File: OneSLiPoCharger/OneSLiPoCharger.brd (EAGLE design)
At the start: 101.6 x 52.1 mm, 55 parts, among them IC1 LM358N, Q1 BUZ10

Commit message: Widen isolation. Add ground traces to MCP groups to account for lack of gnd pour. Reduce board width.
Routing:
- net GND: track 0.00 -> 94.4 mm
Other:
- board size 101.6 x 52.1 mm -> 99.1 x 52.1 mm
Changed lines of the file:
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@@
 <grid distance="0.05" unitdist="inch" unit="inch" style="lines" multiple="1" display="no" altdistance="0.025" altunitdist="inch" altunit="inch"/>
 <layers>
-<layer number="1" name="Top" color="4" fill="1" visible="yes" active="yes"/>
-<layer number="16" name="Bottom" color="1" fill="1" visible="yes" active="yes"/>
-<layer number="17" name="Pads" color="2" fill="1" visible="yes" active="yes"/>
-<layer number="18" name="Vias" color="2" fill="1" visible="yes" active="yes"/>
-<layer number="19" name="Unrouted" color="6" fill="1" visible="yes" active="yes"/>
+<layer number="1" name="Top" color="4" fill="1" visible="no" active="yes"/>
+<layer number="16" name="Bottom" color="1" fill="1" visible="no" active="yes"/>
+<layer number="17" name="Pads" color="2" fill="1" visible="no" active="yes"/>
+<layer number="18" name="Vias" color="2" fill="1" visible="no" active="yes"/>
+<layer number="19" name="Unrouted" color="6" fill="1" visible="no" active="yes"/>
 <layer number="20" name="Dimension" color="15" fill="1" visible="yes" active="yes"/>
-<layer number="21" name="tPlace" color="7" fill="1" visible="yes" active="yes"/>
-<layer number="22" name="bPlace" color="7" fill="1" visible="yes" active="yes"/>
-<layer number="23" name="tOrigins" color="15" fill="1" visible="yes" active="yes"/>
-<layer number="24" name="bOrigins" color="15" fill="1" visible="yes" active="yes"/>
+<layer number="21" name="tPlace" color="7" fill="1" visible="no" active="yes"/>
+<layer number="22" name="bPlace" color="7" fill="1" visible="no" active="yes"/>
+<layer number="23" name="tOrigins" color="15" fill="1" visible="no" active="yes"/>
+<layer number="24" name="bOrigins" color="15" fill="1" visible="no" active="yes"/>
 <layer number="25" name="tNames" color="7" fill="1" visible="no" active="yes"/>
 <layer number="26" name="bNames" color="7" fill="1" visible="no" active="yes"/>
@@
 <layer number="43" name="vRestrict" color="2" fill="10" visible="no" active="yes"/>
 <layer number="44" name="Drills" color="7" fill="1" visible="no" active="yes"/>
-<layer number="45" name="Holes" color="7" fill="1" visible="yes" active="yes"/>
+<layer number="45" name="Holes" color="7" fill="1" visible="no" active="yes"/>
 <layer number="46" name="Milling" color="3" fill="1" visible="no" active="yes"/>
 <layer number="47" name="Measures" color="7" fill="1" visible="no" active="yes"/>
@@
 <board>
 <plain>
-<wire x1="101.6" y1="0" x2="101.6" y2="52.07" width="0" layer="20"/>
-<wire x1="101.6" y1="52.07" x2="0" y2="52.07" width="0" layer="20"/>
+<wire x1="99.06" y1="0" x2="99.06" y2="52.07" width="0" layer="20"/>
+<wire x1="99.06" y1="52.07" x2="0" y2="52.07" width="0" layer="20"/>
 <wire x1="0" y1="52.07" x2="0" y2="0" width="0" layer="20"/>
 <text x="53.34" y="29.21" size="1.016" layer="21" rot="R180">BAT1</text>
@@
 <text x="67.31" y="22.86" size="1.016" layer="21">BAT5</text>
 <text x="86.36" y="22.86" size="1.016" layer="21">BAT6</text>
-<text x="97.79" y="22.86" size="1.778" layer="16" rot="MR90">1SLipo v1.0</text>
+<text x="95.25" y="22.86" size="1.778" layer="16" rot="MR90">1SLipo v1.0</text>
 <hole x="2.54" y="2.54" drill="3.2"/>
 <hole x="2.54" y="49.53" drill="3.2"/>
-<hole x="99.06" y="49.53" drill="3.2"/>
-<hole x="99.06" y="2.54" drill="3.2"/>
-<wire x1="101.6" y1="0" x2="0" y2="0" width="0" layer="20"/>
+<hole x="96.52" y="49.53" drill="3.2"/>
+<hole x="96.52" y="2.54" drill="3.2"/>
+<wire x1="99.06" y1="0" x2="0" y2="0" width="0" layer="20"/>
 </plain>
 <attributes>
@@
 <contactref element="U$1" pad="2"/>
 <contactref element="C3" pad="1"/>
-<polygon width="0.6096" layer="16" isolate="0.3048">
+<polygon width="0.6096" layer="16" isolate="0.6096">
 <vertex x="0" y="0"/>
-<vertex x="101.6" y="0"/>
-<vertex x="101.6" y="52.07"/>
+<vertex x="99.06" y="0"/>
+<vertex x="99.06" y="52.07"/>
 <vertex x="0" y="52.07"/>
 </polygon>
@@
 <contactref element="U$13" pad="P$1"/>
 <contactref element="JP1" pad="3"/>
+<wire x1="50.8" y1="41.59" x2="50.48" y2="41.59" width="0.6096" layer="16"/>
+<wire x1="50.48" y1="41.59" x2="46.99" y2="38.1" width="0.6096" layer="16"/>
+<wire x1="46.99" y1="38.1" x2="46.99" y2="37.78" width="0.6096" layer="16"/>
+<wire x1="46.99" y1="37.78" x2="48.58" y2="37.78" width="0.6096" layer="16"/>
+<wire x1="48.58" y1="37.78" x2="49.53" y2="36.83" width="0.6096" layer="16"/>
+<wire x1="49.53" y1="36.83" x2="53.37" y2="36.83" width="0.6096" layer="16"/>
+<wire x1="53.37" y1="36.83" x2="54.61" y2="36.83" width="0.6096" layer="16"/>
+<wire x1="54.61" y1="36.83" x2="55.88" y2="37.78" width="0.6096" layer="16"/>
+<wire x1="64.77" y1="37.78" x2="64.77" y2="38.1" width="0.6096" layer="16"/>
+<wire x1="64.77" y1="38.1" x2="68.26" y2="41.59" width="0.6096" layer="16"/>
+<wire x1="68.26" y1="41.59" x2="68.58" y2="41.59" width="0.6096" layer="16"/>
+<wire x1="71.15" y1="36.83" x2="67.31" y2="36.83" width="0.6096" layer="16"/>
+<wire x1="67.31" y1="36.83" x2="66.36" y2="37.78" width="0.6096" layer="16"/>
+<wire x1="66.36" y1="37.78" x2="64.77" y2="37.78" width="0.6096" layer="16"/>
+<wire x1="71.15" y1="36.83" x2="72.39" y2="36.83" width="0.6096" layer="16"/>
+<wire x1="72.39" y1="36.83" x2="73.66" y2="37.78" width="0.6096" layer="16"/>
+<wire x1="83.82" y1="37.78" x2="83.82" y2="38.1" width="0.6096" layer="16"/>
+<wire x1="83.82" y1="38.1" x2="87.31" y2="41.59" width="0.6096" layer="16"/>
+<wire x1="87.31" y1="41.59" x2="87.63" y2="41.59" width="0.6096" layer="16"/>
+<wire x1="90.2" y1="36.83" x2="86.36" y2="36.83" width="0.6096" layer="16"/>
+<wire x1="86.36" y1="36.83" x2="85.41" y2="37.78" width="0.6096" layer="16"/>
+<wire x1="85.41" y1="37.78" x2="83.82" y2="37.78" width="0.6096" layer="16"/>
+<wire x1="90.2" y1="36.83" x2="91.44" y2="36.83" width="0.6096" layer="16"/>
+<wire x1="91.44" y1="36.83" x2="92.71" y2="37.78" width="0.6096" layer="16"/>
+<wire x1="93.98" y1="14.29" x2="93.98" y2="13.97" width="0.6096" layer="16"/>
+<wire x1="90.17" y1="10.16" x2="90.17" y2="10.48" width="0.6096" layer="16"/>
+<wire x1="87.6" y1="15.24" x2="86.36" y2="15.24" width="0.6096" layer="16"/>
+<wire x1="86.36" y1="15.24" x2="85.41" y2="14.29" width="0.6096" layer="16"/>
+<wire x1="85.41" y1="14.29" x2="85.09" y2="14.29" width="0.6096" layer="16"/>
+<wire x1="68.55" y1="15.24" x2="67.31" y2="15.24" width="0.6096" layer="16"/>
+<wire x1="67.31" y1="15.24" x2="66.36" y2="14.29" width="0.6096" layer="16"/>
+<wire x1="66.36" y1="14.29" x2="66.04" y2="14.29" width="0.6096" layer="16"/>
+<wire x1="68.55" y1="15.24" x2="72.39" y2="15.24" width="0.6096" layer="16"/>
+<wire x1="72.39" y1="15.24" x2="73.34" y2="14.29" width="0.6096" layer="16"/>
+<wire x1="73.34" y1="14.29" x2="74.93" y2="14.29" width="0.6096" layer="16"/>
+<wire x1="74.93" y1="14.29" x2="74.93" y2="12.7" width="0.6096" layer="16"/>
+<wire x1="74.93" y1="12.7" x2="72.71" y2="10.48" width="0.6096" layer="16"/>
+<wire x1="72.71" y1="10.48" x2="71.12" y2="10.48" width="0.6096" layer="16"/>
+<wire x1="87.6" y1="15.24" x2="91.44" y2="15.24" width="0.6096" layer="16"/>
+<wire x1="91.44" y1="15.24" x2="92.39" y2="14.29" width="0.6096" layer="16"/>
+<wire x1="92.39" y1="14.29" x2="93.98" y2="14.29" width="0.6096" layer="16"/>
+<wire x1="90.17" y1="10.48" x2="90.49" y2="10.16" width="0.6096" layer="16"/>
+<wire x1="90.49" y1="10.16" x2="91.44" y2="10.16" width="0.6096" layer="16"/>
+<wire x1="91.44" y1="10.16" x2="93.98" y2="12.7" width="0.6096" layer="16"/>
+<wire x1="93.98" y1="12.7" x2="93.98" y2="14.29" width="0.6096" layer="16"/>
+<wire x1="50.77" y1="15.24" x2="49.53" y2="15.24" width="0.6096" layer="16"/>
+<wire x1="49.53" y1="15.24" x2="48.58" y2="14.29" width="0.6096" layer="16"/>
+<wire x1="48.58" y1="14.29" x2="48.26" y2="14.29" width="0.6096" layer="16"/>
+<wire x1="50.77" y1="15.24" x2="54.61" y2="15.24" width="0.6096" layer="16"/>
+<wire x1="54.61" y1="15.24" x2="55.56" y2="14.29" width="0.6096" layer="16"/>
+<wire x1="55.56" y1="14.29" x2="57.15" y2="14.29" width="0.6096" layer="16"/>
+<wire x1="57.15" y1="14.29" x2="57.15" y2="12.7" width="0.6096" layer="16"/>
+<wire x1="57.15" y1="12.7" x2="54.93" y2="10.48" width="0.6096" layer="16"/>
+<wire x1="54.93" y1="10.48" x2="53.34" y2="10.48" width="0.6096" layer="16"/>
+<wire x1="88.275159375" y1="33.02" x2="90.2" y2="36.83" width="0" layer="19" extent="16-16"/>
+<wire x1="19.05" y1="29.21" x2="16.51" y2="36.83" width="0" layer="19" extent="1-1"/>
 </signal>
 <signal name="N$1">

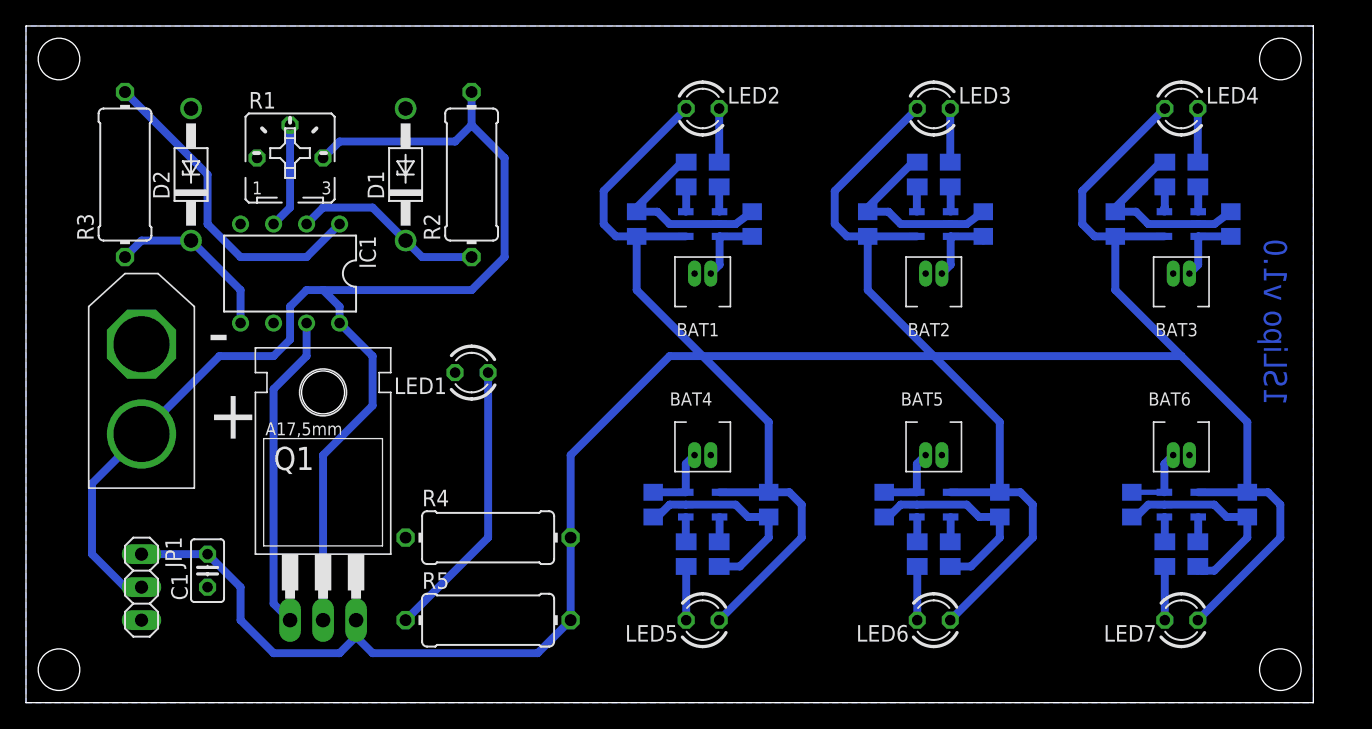
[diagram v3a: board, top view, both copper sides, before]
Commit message: Prep board for OSHPark. Fix feedback on voltage regulator opamp.
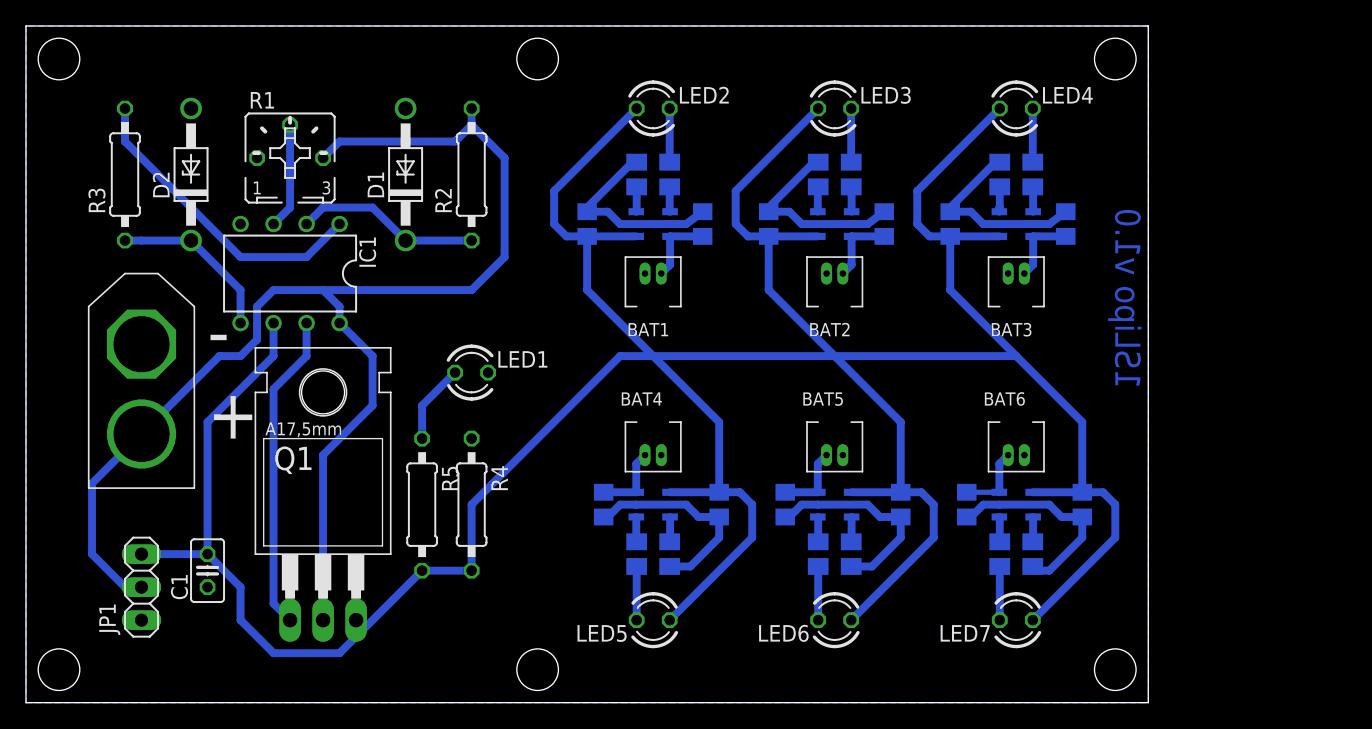
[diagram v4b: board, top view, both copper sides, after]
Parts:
- added DRILEGEND: (no value), drilegend:DRILEGEND
- R2, R3, R4, R5: device rcl:0411/12 -> rcl:0207/10
- moved C12 12.7 mm to (81.3, 15.2)
- moved C13 12.7 mm to (72.4, 15.2)
- moved LED4 12.7 mm to (76.2, 45.7)
- moved LED7 12.7 mm to (76.2, 6.35)
- moved R10 12.7 mm to (77.5, 40.6)
- moved R17 12.7 mm to (77.5, 11.4)
- moved U$12 12.7 mm to (76.2, 15.2)
- moved U$13 12.7 mm to (76.2, 19.1)
- moved U$6 12.7 mm to (76.2, 36.8)
- moved U$7 12.7 mm to (76.2, 33.0)
- moved C6 12.7 mm to (71.1, 36.8)
- moved C7 12.7 mm to (80.0, 36.8)
- moved R11 12.7 mm to (74.9, 40.6)
- moved R16 12.7 mm to (74.9, 11.4)
- moved R5 10.2 mm to (30.5, 15.2), turned to 270 degrees
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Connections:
- net +5V: now also IC1.6
- net GND: no longer IC1.6
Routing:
- net N$10: track 21.7 -> 6.13 mm
- net +5V: track 285.0 -> 286.7 mm
- net VCC: track 105.5 -> 104.3 mm
- net N$4: track 25.1 -> 23.8 mm
- net N$3: track 14.8 -> 14.3 mm
- net N$2: track 13.5 -> 13.0 mm
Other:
- board size 99.1 x 52.1 mm -> 86.4 x 52.1 mm
- board text added: "01-16"
- board text added: "01-20"
- board text added: "LAYER-STACK"

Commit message: Fix miswired input on first opamp. Add a positive feedback volage divider for some hysteresis.
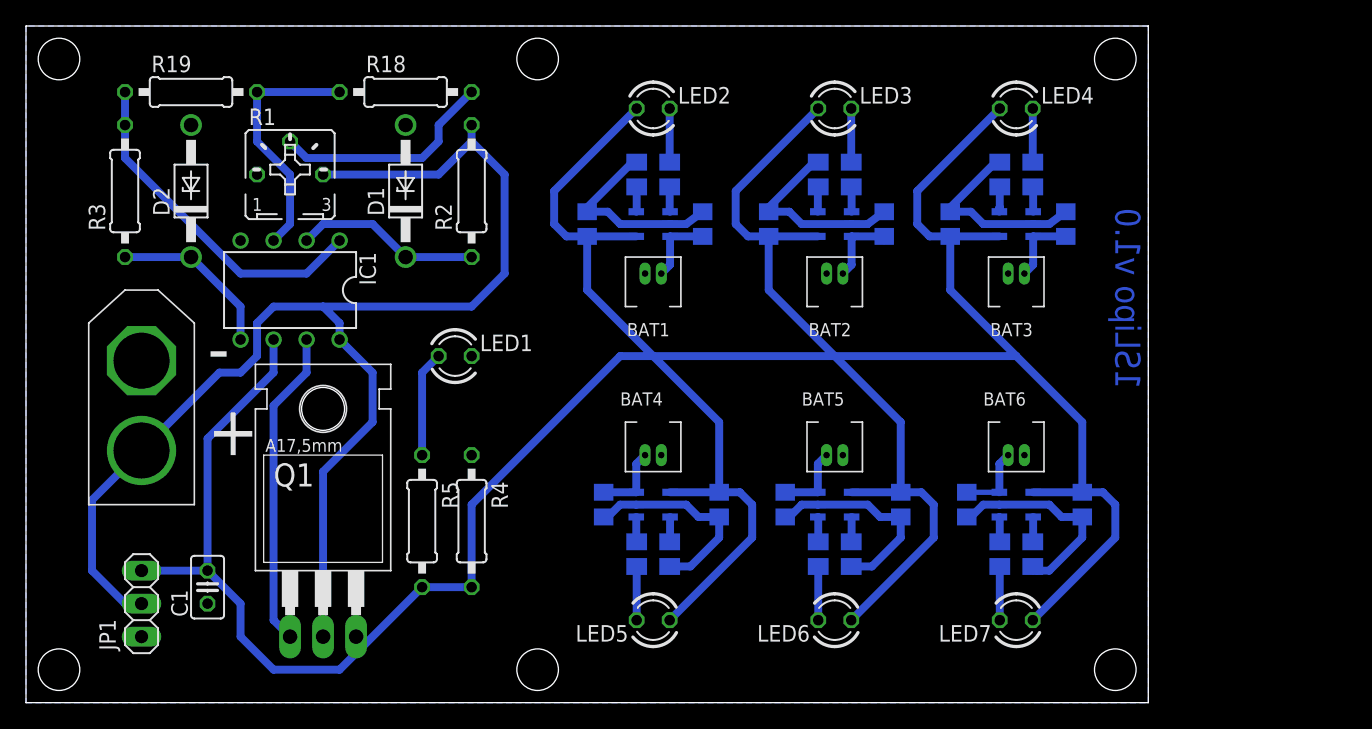
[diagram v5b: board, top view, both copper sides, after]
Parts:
- added R18: 1K, rcl:0207/10
- added R19: 470K, rcl:0207/10
- moved LED1 1.80 mm to (33.0, 26.7)
- moved D1 1.27 mm to (29.2, 39.4)
- moved D2 1.27 mm to (12.7, 39.4)
- moved IC1 1.27 mm to (20.3, 31.8)
- moved R2 1.27 mm to (34.3, 39.4)
- moved R3 1.27 mm to (7.62, 39.4)
- moved JP1 1.27 mm to (8.89, 7.62)
- moved C1 1.27 mm to (14.0, 8.89)
- moved Q1 1.27 mm to (22.9, 11.4)
- moved R4 1.27 mm to (34.3, 14.0)
- moved R5 1.27 mm to (30.5, 14.0)
- moved U$3 1.27 mm to (8.89, 22.9)
- moved R1 1.27 mm to (20.3, 40.6)
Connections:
- new net N$31: IC1.3, R18.1, R19.2
- net N$1: now also R18.2; no longer IC1.3
- net N$4: now also R19.1
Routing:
- net N$31: track 0.00 -> 19.4 mm
- net N$1: track 8.15 -> 17.3 mm
- net N$4: track 23.8 -> 26.3 mm
- net N$10: track 6.13 -> 8.15 mm
- net +5V: track 286.7 -> 287.9 mm
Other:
- board text removed: "01-16"
- board text removed: "01-20"
- board text removed: "LAYER-STACK"
